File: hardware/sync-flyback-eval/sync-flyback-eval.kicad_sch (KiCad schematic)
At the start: 94 parts, among them J1 RJ45_LED_Shielded, Q1 SiR422DP, Q2 Si7898DP, Q3 MMDT3906, T1 PoE_Transformer, T2 Pulse_Transformer, U1 TPS23754PWPR, U2 TCMT1107

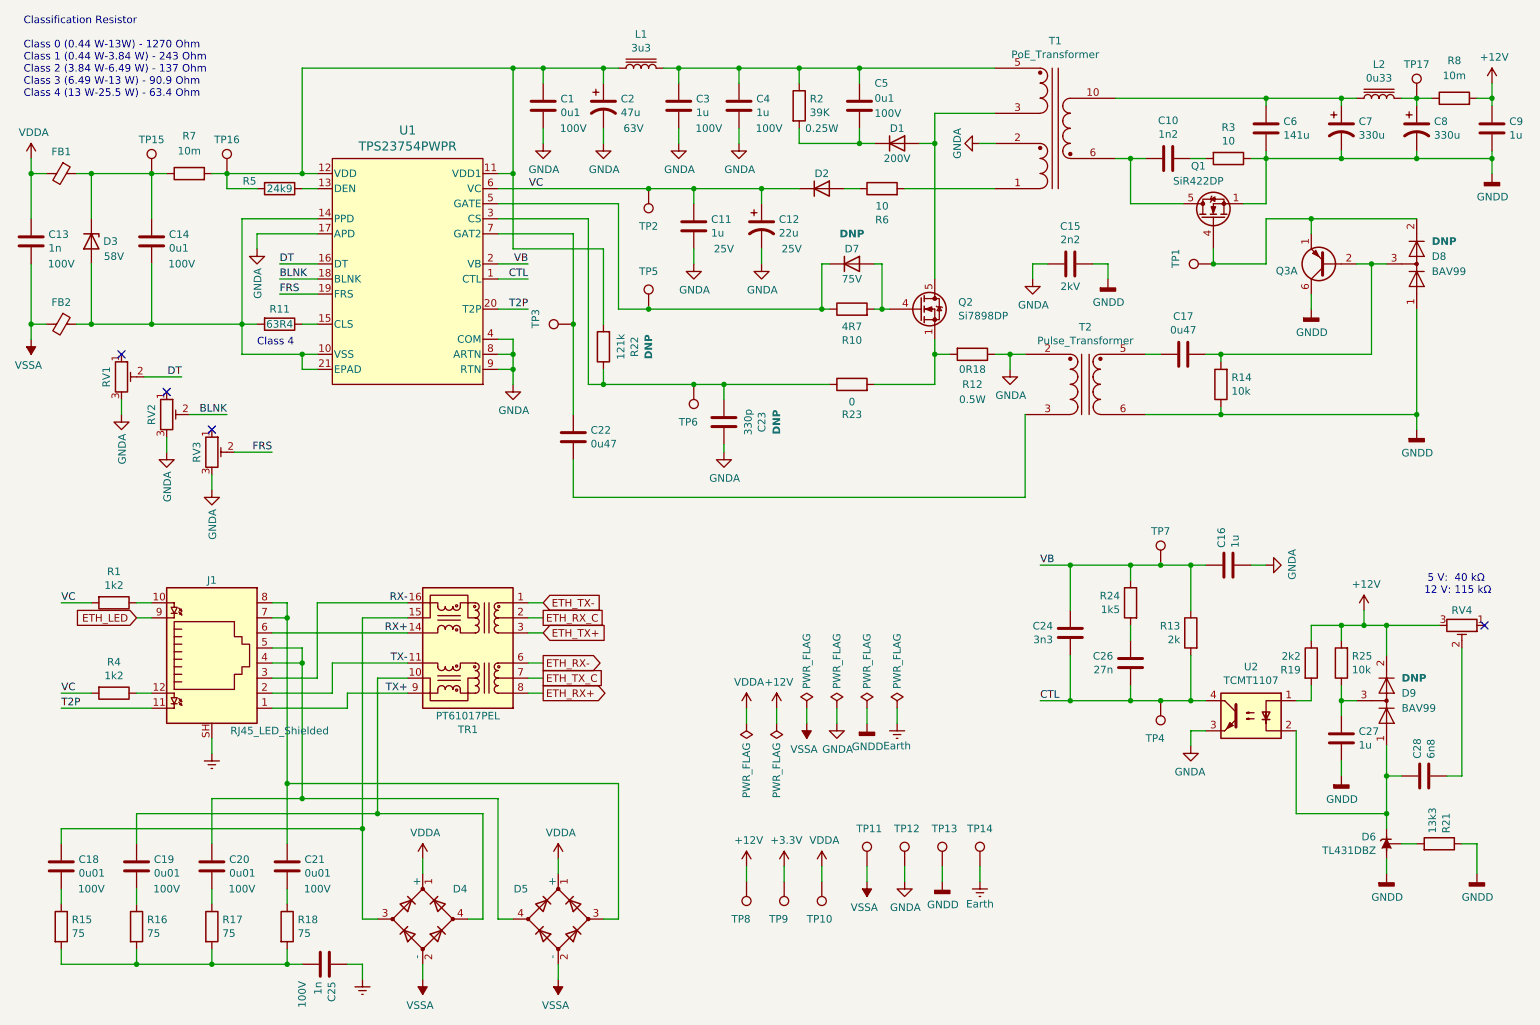
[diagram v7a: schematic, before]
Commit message: flyback: address ERC results
This came down to updating the library references (this was a result
of the migration to KiCad 6), adding a power flag to VSS, and marking
the Ethernet pins "no connection".
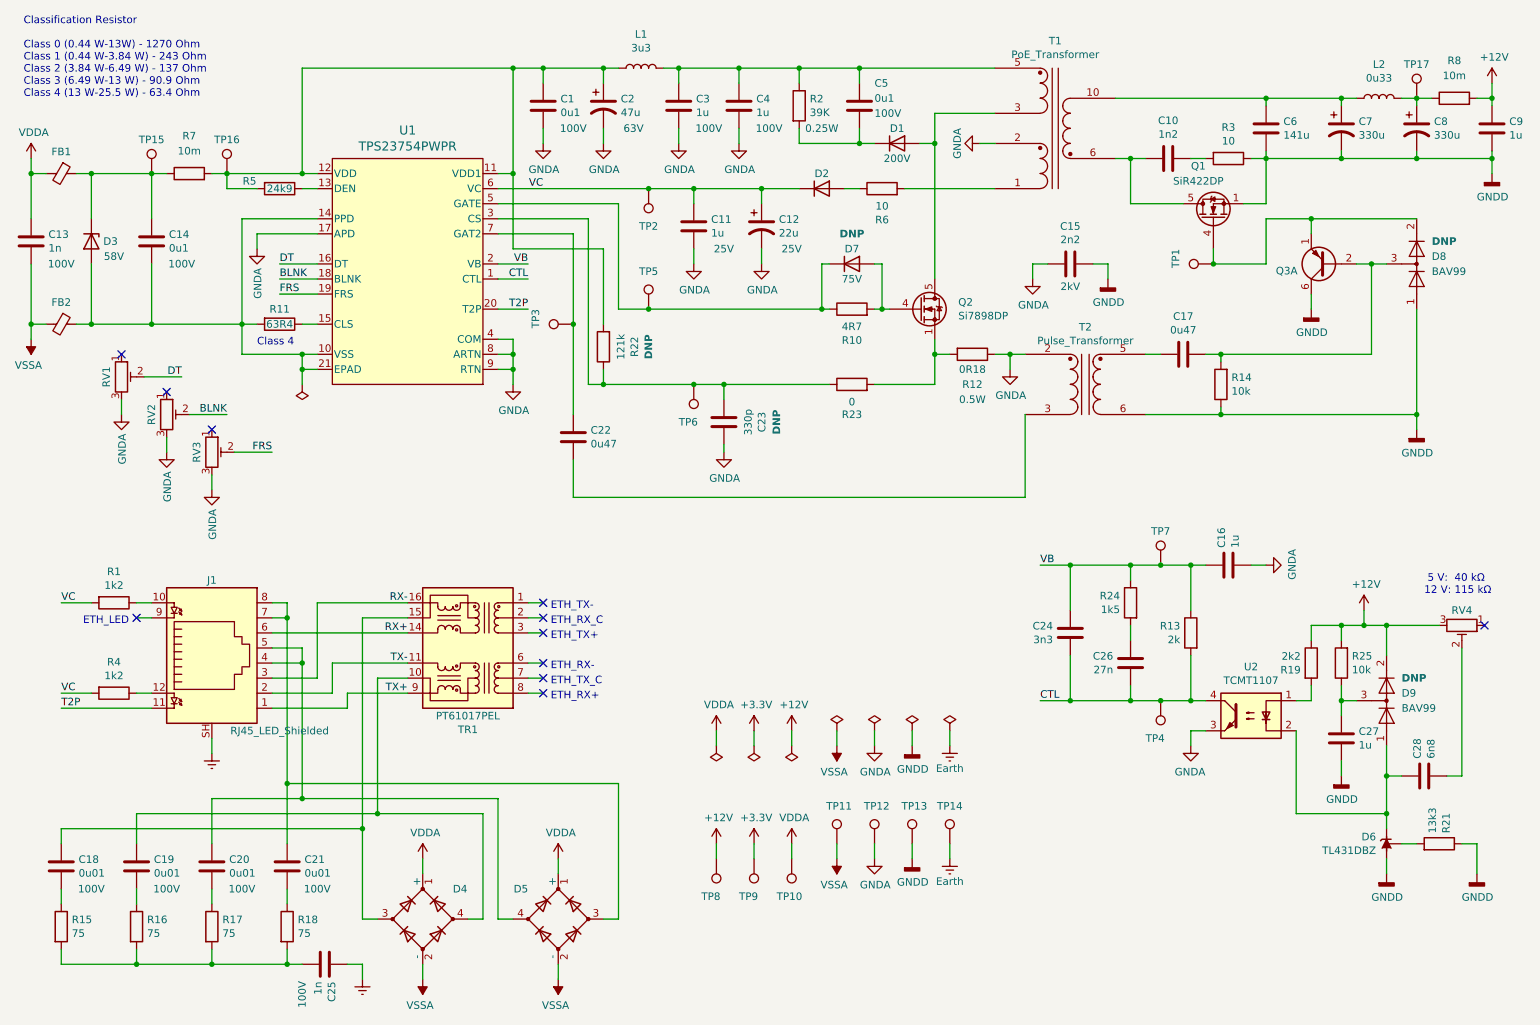
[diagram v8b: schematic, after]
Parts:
- C12, C2, C7, C8: symbol Device:CP1 -> Device:C_Polarized_US
- FB1, FB2: symbol Device:Ferrite_Bead_Small -> Device:FerriteBead_Small
- L1, L2: symbol Device:L_Core_Iron -> Device:L
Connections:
- net ETH_LED: no longer names the net of J1.9
- net ETH_RX+: no longer names the net of TR1.8 (RD-)
- net ETH_RX-: no longer names the net of TR1.6 (RD+)
- net ETH_RX_C: no longer names the net of TR1.2 (C_TD)
- net ETH_TX+: no longer names the net of TR1.3 (TD-)
- net ETH_TX-: no longer names the net of TR1.1 (TD+)
- net ETH_TX_C: no longer names the net of TR1.7 (C_RD)
- no-connect marks 4 -> 11
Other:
- note added: "ETH_LED"
- note added: "ETH_RX+"
- note added: "ETH_RX-"
- note added: "ETH_RX_C"
- note added: "ETH_TX+"
- note added: "ETH_TX-"
- note added: "ETH_TX_C"
- moved on the sheet: TP10, TP11, TP12, TP13, TP14, TP8, TP9
